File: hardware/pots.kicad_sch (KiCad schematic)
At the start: 4 parts, among them J16 Conn_01x03, J17 Conn_01x03

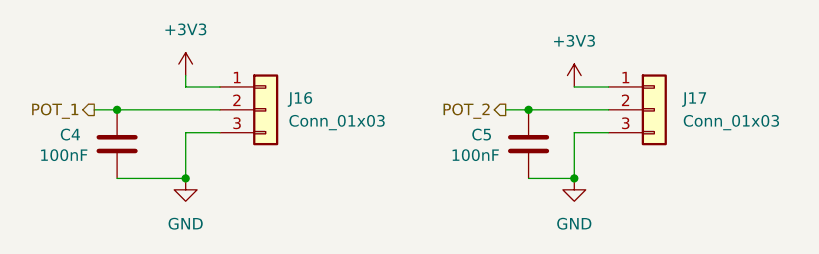
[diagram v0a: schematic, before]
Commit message: place the stuff on the pcb
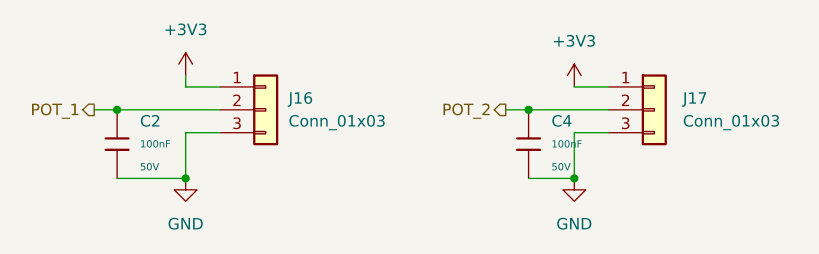
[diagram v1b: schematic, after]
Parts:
- removed C4, C5: 100nF, symbol Device:C
- added C2, C4: 100nF, PCM_JLCPCB:C_0402, symbol PCM_JLCPCB-Capacitors:0402,100nF,(2)
- J16, J17: footprint (none) -> Connector_JST:JST_XH_B3B-XH-A_1x03_P2.50mm_Vertical
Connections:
- net GND: now also C2.2, C4.2
- net POT_1: now also C2.1
- net POT_2: now also C4.1
